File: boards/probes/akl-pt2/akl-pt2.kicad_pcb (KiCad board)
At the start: 2 copper layers, 150.5 x 8 mm, 6 parts, among them J1 SMA, J2 TIP, J3 GND

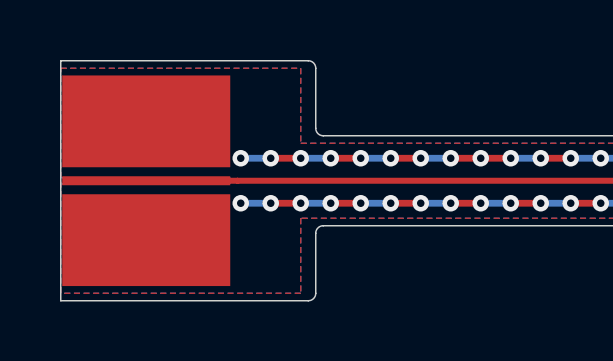
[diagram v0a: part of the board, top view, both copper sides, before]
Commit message: AKL-PT2 v0.5c with extra vias
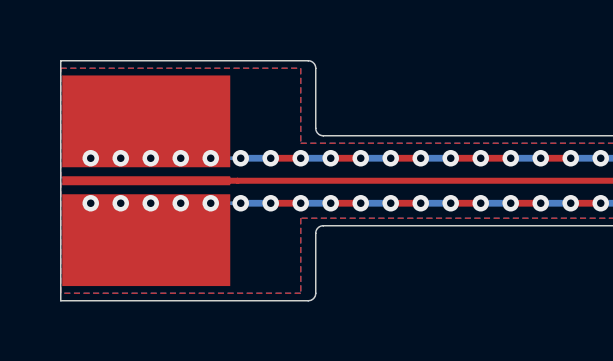
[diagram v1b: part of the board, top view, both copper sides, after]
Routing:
- net /GND: track 285.3 -> 295.3 mm, vias 286 -> 296
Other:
- board text added: "AKL-PT2 / A. Zonenberg / Antikernel Labs / Symbiotic EDA / v0.5c / 2020-12-25"
- board text removed: "AKL-PT2 / A. Zonenberg / Antikernel Labs / Symbiotic EDA / v0.5 / 2020-12-22"
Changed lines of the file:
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@@
     (thickness 0.23)
     (drawings 25)
-    (tracks 583)
+    (tracks 603)
     (zones 0)
     (modules 6)
@@
     (39 F.Mask user)
     (40 Dwgs.User user)
-    (42 Eco1.User user)
+    (42 Eco1.User user hide)
     (43 Eco2.User user)
     (44 Edge.Cuts user)
@@
   (gr_arc (start 236.75 49) (end 237 49) (angle -90) (layer Edge.Cuts) (width 0.05))
   (gr_line (start 95.25 48.75) (end 236.75 48.75) (layer Edge.Cuts) (width 0.05))
-  (gr_text "AKL-PT2 / A. Zonenberg / Antikernel Labs / Symbiotic EDA / v0.5 / 2020-12-22" (at 127 50.25) (layer B.SilkS)
+  (gr_text "AKL-PT2 / A. Zonenberg / Antikernel Labs / Symbiotic EDA / v0.5c / 2020-12-25" (at 127 50.25) (layer B.SilkS)
     (effects (font (size 1 1) (thickness 0.15)) (justify mirror))
   )
@@
   (via (at 236.95 50.75) (size 0.55) (drill 0.25) (layers F.Cu B.Cu) (net 1))
   (segment (start 236.45 50.75) (end 237 50.75) (width 0.125) (layer F.Cu) (net 1))
+  (via (at 91.5 49.5) (size 0.55) (drill 0.25) (layers F.Cu B.Cu) (net 1))
+  (segment (start 92.5 49.5) (end 91.5 49.5) (width 0.125) (layer B.Cu) (net 1))
+  (via (at 90.5 49.5) (size 0.55) (drill 0.25) (layers F.Cu B.Cu) (net 1))
+  (segment (start 91.5 49.5) (end 90.5 49.5) (width 0.125) (layer B.Cu) (net 1))
+  (via (at 89.5 49.5) (size 0.55) (drill 0.25) (layers F.Cu B.Cu) (net 1))
+  (segment (start 90.5 49.5) (end 89.5 49.5) (width 0.125) (layer F.Cu) (net 1))
+  (via (at 88.5 49.5) (size 0.55) (drill 0.25) (layers F.Cu B.Cu) (net 1))
+  (segment (start 89.5 49.5) (end 88.5 49.5) (width 0.125) (layer B.Cu) (net 1))
+  (via (at 87.5 49.5) (size 0.55) (drill 0.25) (layers F.Cu B.Cu) (net 1))
+  (segment (start 88.5 49.5) (end 87.5 49.5) (width 0.125) (layer F.Cu) (net 1))
+  (via (at 91.5 51) (size 0.55) (drill 0.25) (layers F.Cu B.Cu) (net 1))
+  (segment (start 92.5 51) (end 91.5 51) (width 0.125) (layer B.Cu) (net 1))
+  (via (at 90.5 51) (size 0.55) (drill 0.25) (layers F.Cu B.Cu) (net 1))
+  (segment (start 91.5 51) (end 90.5 51) (width 0.125) (layer F.Cu) (net 1))
+  (via (at 89.5 51) (size 0.55) (drill 0.25) (layers F.Cu B.Cu) (net 1))
+  (segment (start 90.5 51) (end 89.5 51) (width 0.125) (layer B.Cu) (net 1))
+  (via (at 88.5 51) (size 0.55) (drill 0.25) (layers F.Cu B.Cu) (net 1))
+  (segment (start 89.5 51) (end 88.5 51) (width 0.125) (layer F.Cu) (net 1))
+  (via (at 87.5 51) (size 0.55) (drill 0.25) (layers F.Cu B.Cu) (net 1))
+  (segment (start 88.5 51) (end 87.5 51) (width 0.125) (layer B.Cu) (net 1))
   (segment (start 231.9 49.95) (end 231.6 50.25) (width 0.2) (layer F.Cu) (net 2))
   (segment (start 232.4 49.95) (end 231.9 49.95) (width 0.2) (layer F.Cu) (net 2))
